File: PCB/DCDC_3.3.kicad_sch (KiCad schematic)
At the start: 18 parts, among them U11 LV2842XLVDDCR

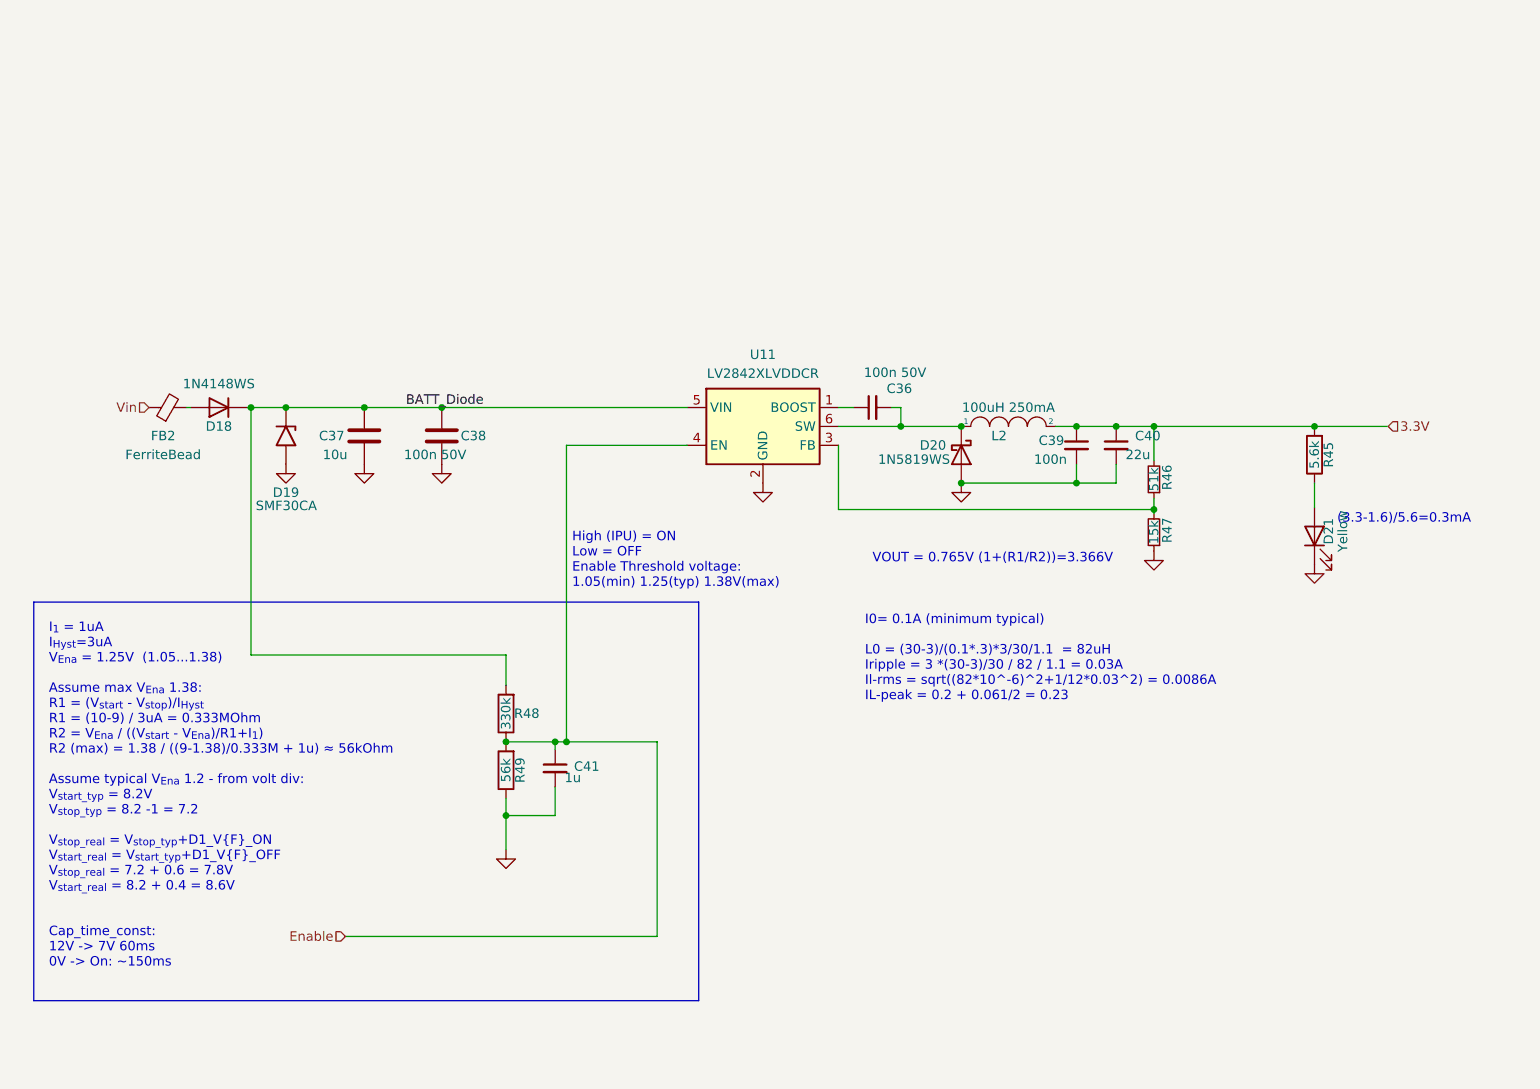
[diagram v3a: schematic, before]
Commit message: ability to fully shutdown on low voltage. Power back on above 11V.
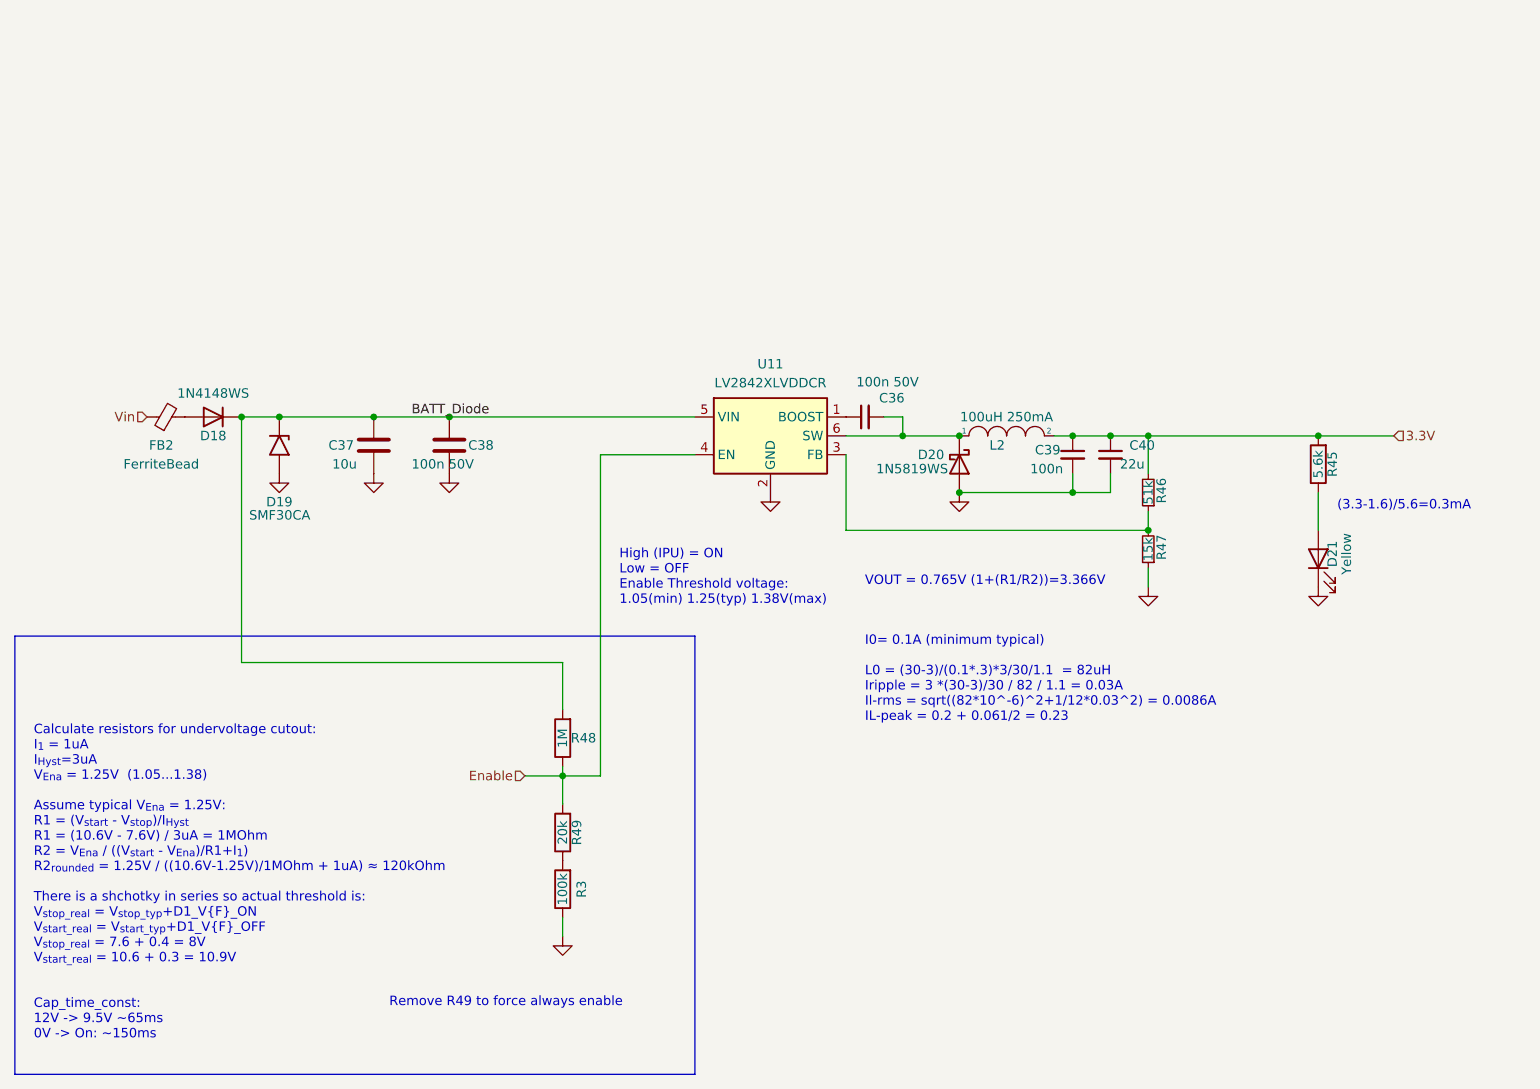
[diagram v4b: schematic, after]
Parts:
- removed C41: 1u, Capacitor_SMD:C_0402_1005Metric, symbol Device:C_Small
- added R3: 100k, Resistor_SMD:R_0402_1005Metric, symbol Device:R
- R48: value 330k -> 1M; LCSC C25778 -> C26083
- R49: value 56k -> 20k; LCSC C25796 -> C25765
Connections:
- net GND: now also R3.1; no longer R49.1
- new net: R3.2, R49.1
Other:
- note added: "Calculate resistors for undervoltage cutout: I_{1} = 1uA I_{Hyst}=3uA V_{Ena} = 1.25V (1.05...1.38) Assume typical V_{Ena} = 1.25V: R1 = (V_{start} - V_{stop})/I_{Hyst} R1 = (10.6V - 7.6V) / 3uA = 1MOhm R2 = V_{Ena} / ((V_{start} - V_{Ena})/R1+I_{1}) R2_{rounded} = 1.25V / ((10.6V-1.25V)/1MOhm + 1uA) ≈ 120kOhm There is a shchotky in series so actual threshold is: V_{stop_real} = V_{stop_typ}+D1_V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"
- note added: "Remove R49 to force always enable"
- note removed: "I_{1} = 1uA I_{Hyst}=3uA V_{Ena} = 1.25V (1.05...1.38) Assume max V_{Ena} 1.38: R1 = (V_{start} - V_{stop})/I_{Hyst} R1 = (10-9) / 3uA = 0.333MOhm R2 = V_{Ena} / ((V_{start} - V_{Ena})/R1+I_{1}) R2 (max) = 1.38 / ((9-1.38)/0.333M + 1u) ≈ 56kOhm Assume typical V_{Ena} 1.2 - from volt div: V_{start_typ} = 8.2V V_{stop_typ} = 8.2 -1 = 7.2 V_{stop_real} = V_{stop_typ}+D1_V{F}_ON V_{start_real} = V_{s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"
- moved on the sheet: C36, C37, C38, C39, C40, D18, D19, D20, D21, FB2, L2, R45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

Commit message: Removed dead properties.  Found alternative Parts D1, D22, R27.  PEDSCAN uses SOT323-3 footprint now
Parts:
- C36, C38: Part CL05B104KB54PNC -> (none)
- C37: Part GRM21BR61H106KE43L -> (none)
- FB2: MFR.Part # GZ1608D601TF -> (none)

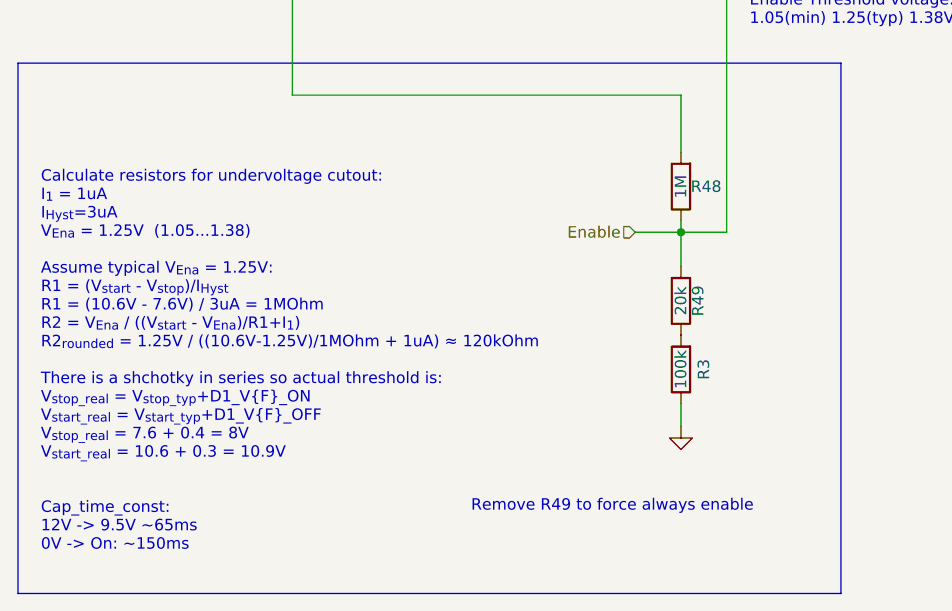
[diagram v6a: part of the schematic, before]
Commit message: Removed DCDC enable control
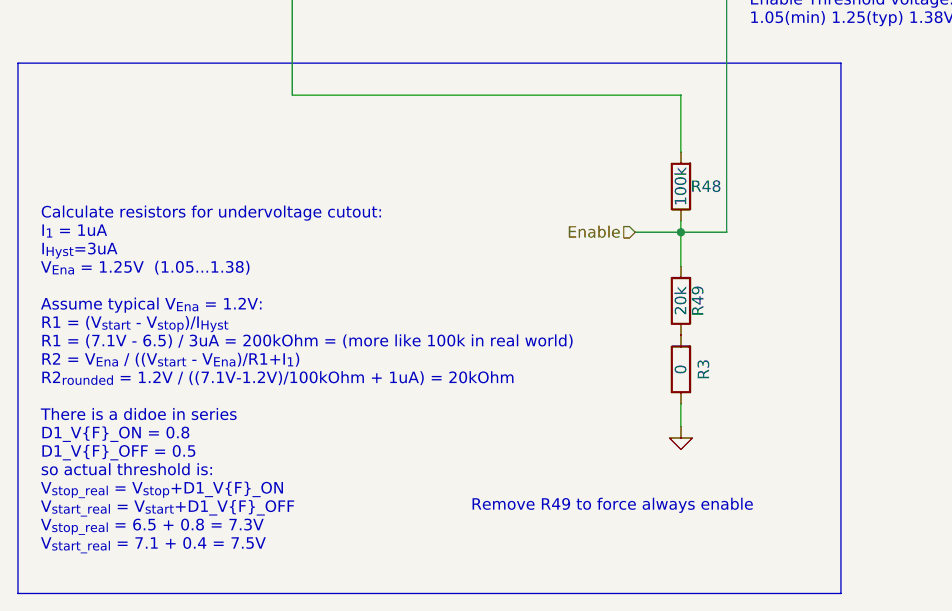
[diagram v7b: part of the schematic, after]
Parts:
- R3: value 100k -> 0; LCSC C25741 -> (none)
- R48: value 1M -> 100k; LCSC C26083 -> C25741
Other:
- note added: "Calculate resistors for undervoltage cutout: I_{1} = 1uA I_{Hyst}=3uA V_{Ena} = 1.25V (1.05...1.38) Assume typical V_{Ena} = 1.2V: R1 = (V_{start} - V_{stop})/I_{Hyst} R1 = (7.1V - 6.5) / 3uA = 200kOhm = (more like 100k in real world) R2 = V_{Ena} / ((V_{start} - V_{Ena})/R1+I_{1}) R2_{rounded} = 1.2V / ((7.1V-1.2V)/100kOhm + 1uA) = 20kOhm There is a didoe in series D1_V{F}_ON = 0.8 D1_V{F}_OFF =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"
- note removed: "Calculate resistors for undervoltage cutout: I_{1} = 1uA I_{Hyst}=3uA V_{Ena} = 1.25V (1.05...1.38) Assume typical V_{Ena} = 1.25V: R1 = (V_{start} - V_{stop})/I_{Hyst} R1 = (10.6V - 7.6V) / 3uA = 1MOhm R2 = V_{Ena} / ((V_{start} - V_{Ena})/R1+I_{1}) R2_{rounded} = 1.25V / ((10.6V-1.25V)/1MOhm + 1uA) ≈ 120kOhm There is a shchotky in series so actual threshold is: V_{stop_real} = V_{stop_typ}+D1_V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"
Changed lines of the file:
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@@
 		)
 	)
-	(text "Calculate resistors for undervoltage cutout:\nI_{1} = 1uA\nI_{Hyst}=3uA\nV_{Ena} = 1.25V  (1.05...1.38)\n\nAssume typical V_{Ena} = 1.25V:\nR1 = (V_{start} - V_{stop})/I_{Hyst}\nR1 = (10.6V - 7.6V) / 3uA = 1MOhm\nR2 = V_{Ena} / ((V_{start} - V_{Ena})/R1+I_{1})\nR2_{rounded} = 1.25V / ((10.6V-1.25V)/1MOhm + 1uA) ≈ 120kOhm\n\nThere is a shchotky in series so actual threshold is:\nV_{stop_real} = V_{stop_typ}+D1_V{F}_ON\nV_{start_real} = V_{start_typ}+D1_V{F}_OFF\nV_{stop_real} = 7.6 + 0.4 = 8V\nV_{start_real} = 10.6 + 0.3 = 10.9V\n\n\nCap_time_const:\n12V -> 9.5V ~65ms\n0V -> On: ~150ms"
+	(text "Calculate resistors for undervoltage cutout:\nI_{1} = 1uA\nI_{Hyst}=3uA\nV_{Ena} = 1.25V  (1.05...1.38)\n\nAssume typical V_{Ena} = 1.2V:\nR1 = (V_{start} - V_{stop})/I_{Hyst}\nR1 = (7.1V - 6.5) / 3uA = 200kOhm = (more like 100k in real world)\nR2 = V_{Ena} / ((V_{start} - V_{Ena})/R1+I_{1})\nR2_{rounded} = 1.2V / ((7.1V-1.2V)/100kOhm + 1uA) = 20kOhm\n\nThere is a didoe in series\nD1_V{F}_ON = 0.8\nD1_V{F}_OFF = 0.5\nso actual threshold is:\nV_{stop_real} = V_{stop}+D1_V{F}_ON\nV_{start_real} = V_{start}+D1_V{F}_OFF\nV_{stop_real} = 6.5 + 0.8 = 7.3V\nV_{start_real} = 7.1 + 0.4 = 7.5V"
 		(exclude_from_sim no)
 		(at 38.1 165.1 0)
@@
 			)
 			(justify left bottom)
-			(href "https://everycircuit.com/circuit/6478510418558976")
 		)
 	)
@@
 	(label "BATT_Diode"
 		(at 88.9 81.28 0)
-		(fields_autoplaced yes)
 		(effects
 			(font
@@
 		(shape input)
 		(at 53.34 81.28 180)
-		(fields_autoplaced yes)
 		(effects
 			(font
@@
 		(shape input)
 		(at 220.98 83.82 0)
-		(fields_autoplaced yes)
 		(effects
 			(font
@@
 		(shape input)
 		(at 104.14 129.54 180)
-		(fields_autoplaced yes)
 		(effects
 			(font
@@
 			)
 		)
-		(property "Value" "100k"
+		(property "Value" "0"
 			(at 109.22 144.78 90)
 			(effects
@@
 			)
 		)
-		(property "LCSC" "C25741"
+		(property "LCSC" ""
 			(at 106.68 145.415 0)
 			(effects
@@
 			)
 		)
-		(property "Value" "1M"
+		(property "Value" "100k"
 			(at 109.22 124.46 90)
 			(effects
@@
 			)
 		)
-		(property "LCSC" "C26083"
+		(property "LCSC" "C25741"
 			(at 106.68 124.46 0)
 			(effects
